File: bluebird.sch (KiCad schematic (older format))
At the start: 34 parts, among them J1 USB_C_Receptacle_USB2.0, J3 Conn_01x05, J4 Conn_01x01, J5 Conn_01x01, J6 AVR-ISP-6, J7 Conn_01x04, SW1 SW_PUSH, U1 ATMEGA32U4, U2 MCP23017_SS, U3 IS31FL3731-SA, Y1 FA328 16MHz

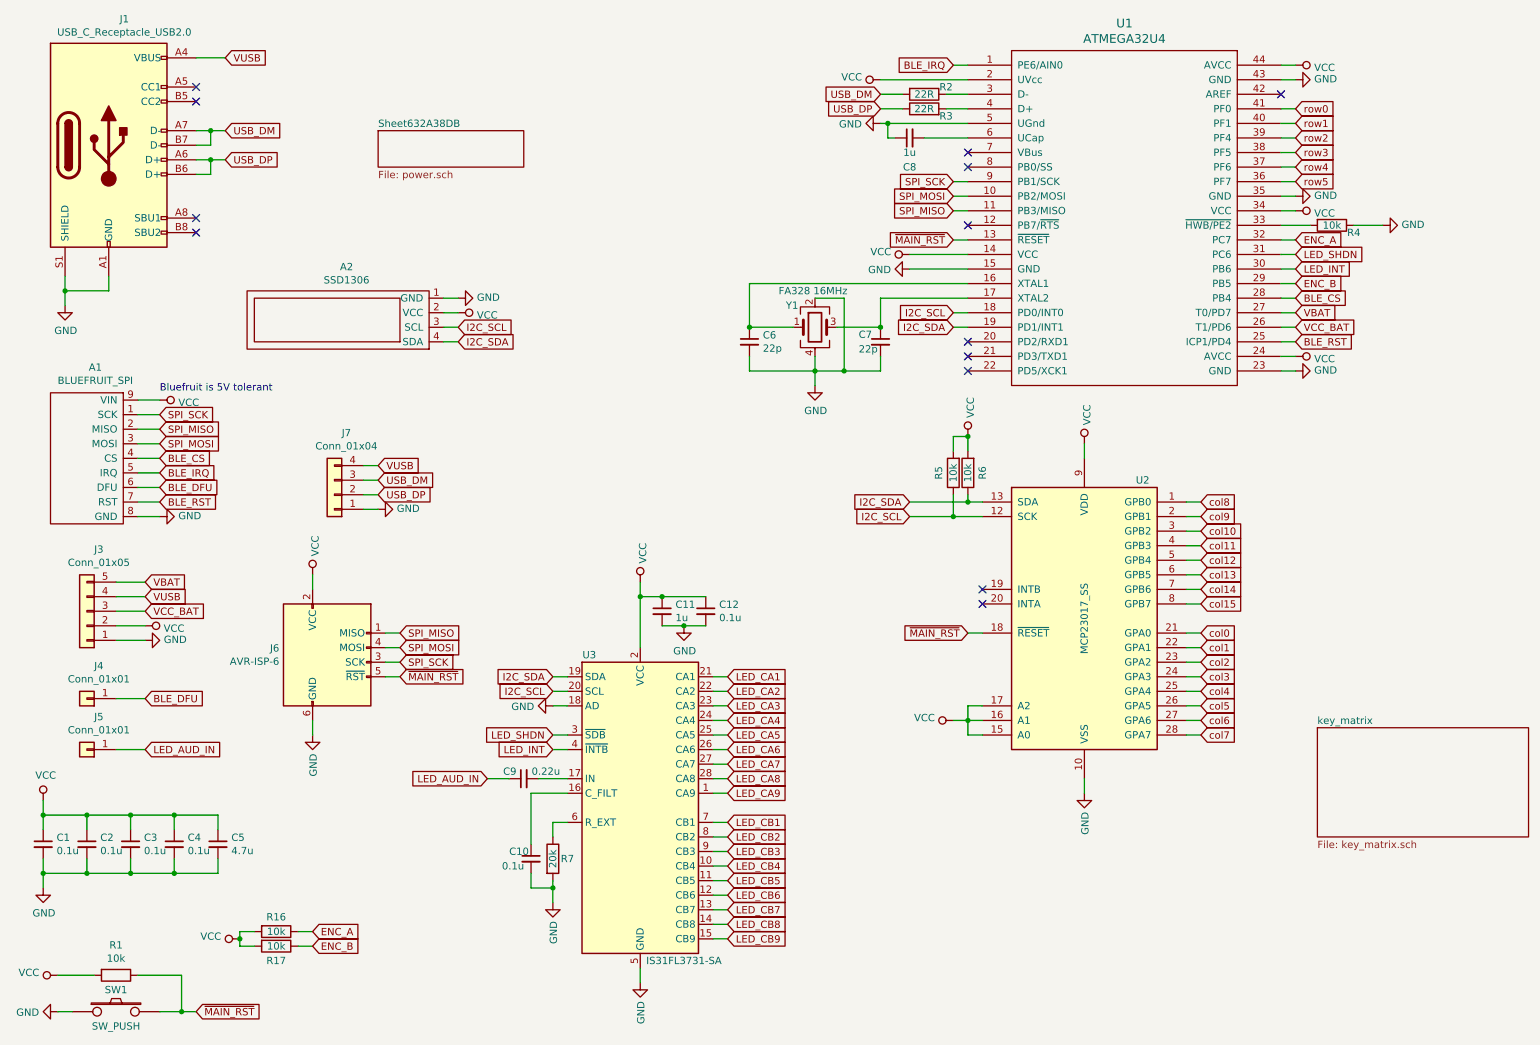
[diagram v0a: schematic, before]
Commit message: Rewire as 2 layer numpad
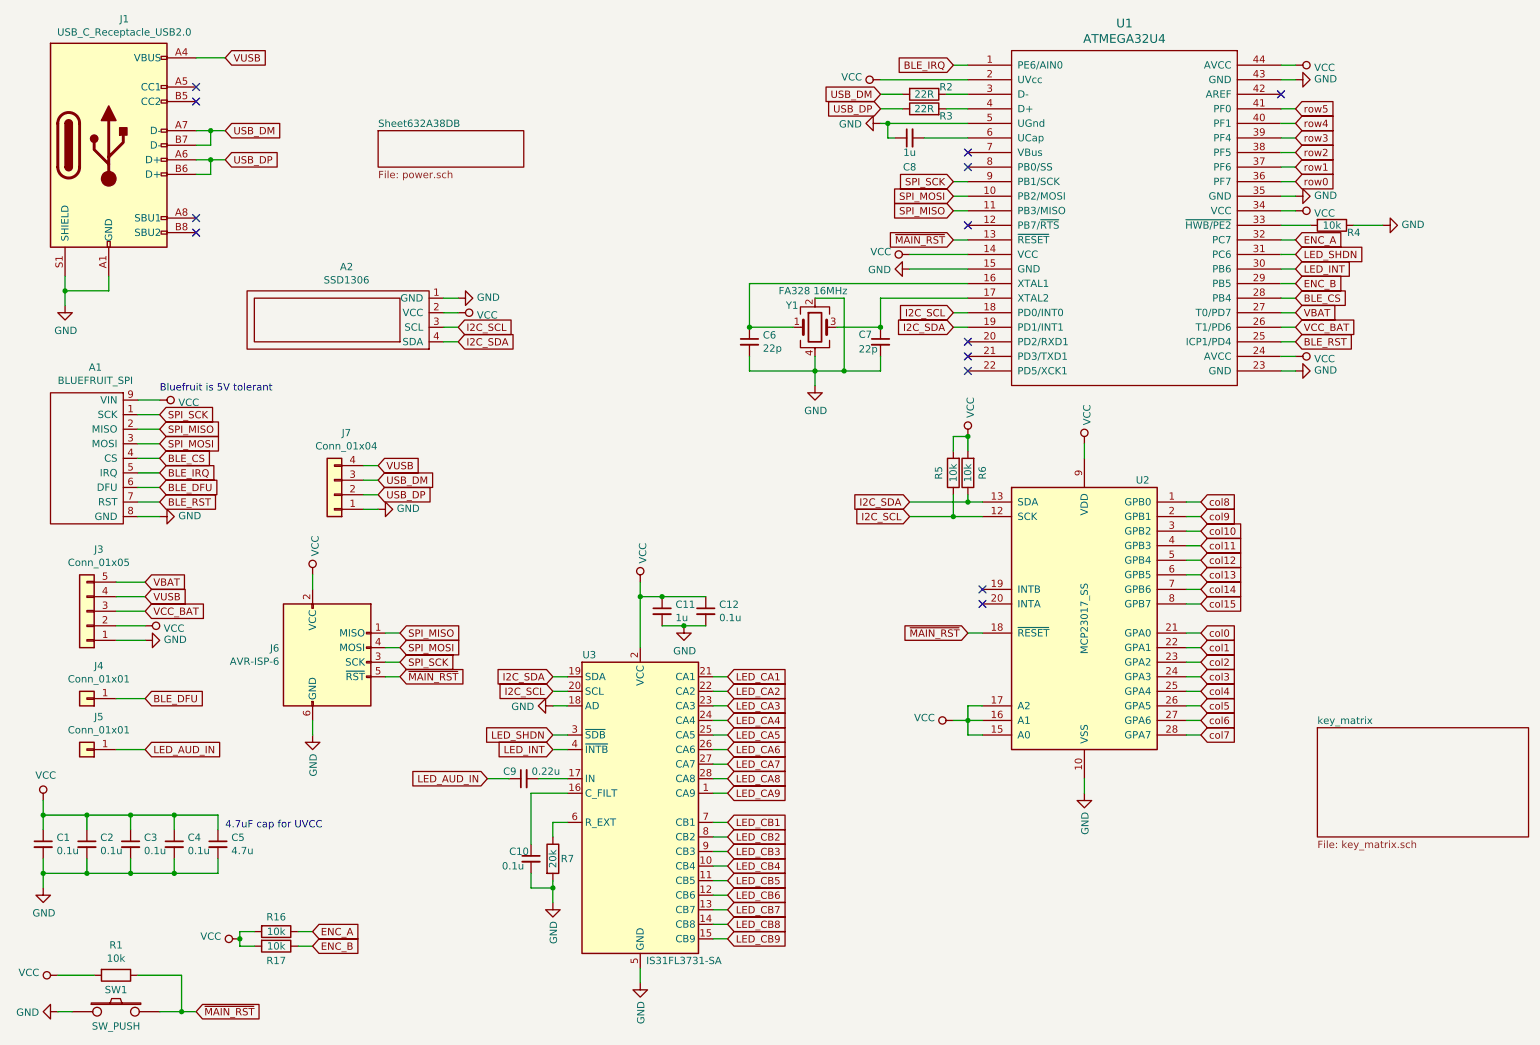
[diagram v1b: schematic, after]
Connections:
- net row0: now also U1.36 (PF7); no longer U1.41 (PF0)
- net row1: now also U1.37 (PF6); no longer U1.40 (PF1)
- net row2: now also U1.38 (PF5); no longer U1.39 (PF4)
- net row3: now also U1.39 (PF4); no longer U1.38 (PF5)
- net row4: now also U1.40 (PF1); no longer U1.37 (PF6)
- net row5: now also U1.41 (PF0); no longer U1.36 (PF7)
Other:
- note added: "4.7uF cap for UVCC"
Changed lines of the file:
@@
 F1 "key_matrix.sch" 50
 $EndSheet
-Text GLabel 9400 1500 2    50   Input ~ 0
+Text GLabel 9400 1800 2    50   Input ~ 0
 row1
 Wire Wire Line
@@
 	1    0    0    -1
 $EndComp
+Text GLabel 9400 1700 2    50   Input ~ 0
+row2
 Text GLabel 9400 1600 2    50   Input ~ 0
-row2
-Text GLabel 9400 1700 2    50   Input ~ 0
 row3
-Text GLabel 9400 1800 2    50   Input ~ 0
+Text GLabel 9400 1500 2    50   Input ~ 0
 row4
-Text GLabel 9400 1900 2    50   Input ~ 0
+Text GLabel 9400 1400 2    50   Input ~ 0
 row5
 Wire Wire Line
@@
 Wire Wire Line
 	7050 5600 7150 5600
-Text GLabel 9400 1400 2    50   Input ~ 0
+Text GLabel 9400 1900 2    50   Input ~ 0
 row0
 $Comp
@@
 Wire Wire Line
 	9300 2900 9400 2900
+Text Notes 2050 6350 0    50   ~ 0
+4.7uF cap for UVCC
 $EndSCHEMATC

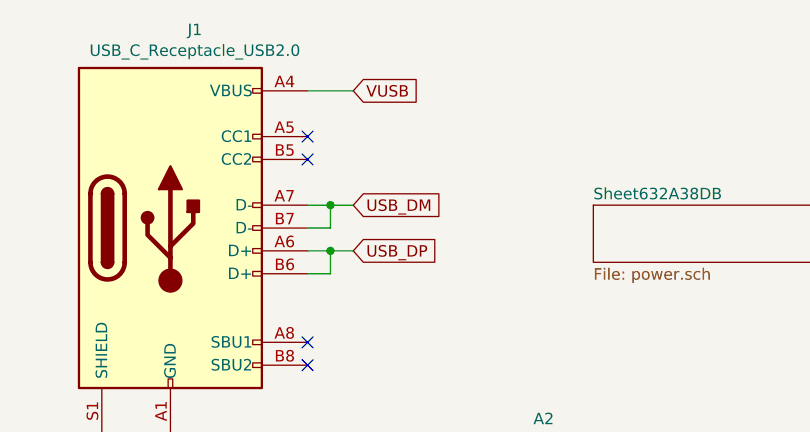
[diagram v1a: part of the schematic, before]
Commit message: Add USB C CC1/CC2 resistors, fix net overlaps.
Add labels to testpoints.
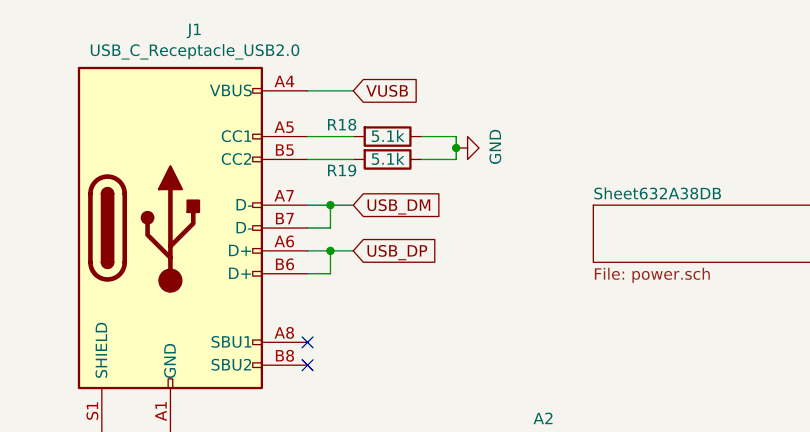
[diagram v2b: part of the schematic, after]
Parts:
- added R18, R19: 5.1k, Resistor_SMD:R_0805_2012Metric_Pad1.15x1.40mm_HandSolder, symbol Device:R
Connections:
- net GND: now also R18.1, R19.1
- net at J1.A5 (CC1): now also R18.2
- net at J1.B5 (CC2): now also R19.2
- no-connect marks 13 -> 11
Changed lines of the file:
@@
 NoConn ~ 1850 2150
 NoConn ~ 1850 2250
-NoConn ~ 1850 1350
-NoConn ~ 1850 1250
 Wire Wire Line
 	4300 5700 4400 5700
@@
 Text Notes 2050 6350 0    50   ~ 0
 4.7uF cap for UVCC
+$Comp
+L Device:R R18
+U 1 1 5EE4669E
+P 2200 1250
+F 0 "R18" V 2150 1050 50  0000 C CNN
+F 1 "5.1k" V 2200 1250 50  0000 C CNN
+F 2 "Resistor_SMD:R_0805_2012Metric_Pad1.15x1.40mm_HandSolder" V 2130 1250 50  0001 C CNN
+F 3 "~" H 2200 1250 50  0001 C CNN
+	1    2200 1250
+	0    1    1    0
+$EndComp
+$Comp
+L Device:R R19
+U 1 1 5EE46F2F
+P 2200 1350
+F 0 "R19" V 2250 1150 50  0000 C CNN
+F 1 "5.1k" V 2200 1350 50  0000 C CNN
+F 2 "Resistor_SMD:R_0805_2012Metric_Pad1.15x1.40mm_HandSolder" V 2130 1350 50  0001 C CNN
+F 3 "~" H 2200 1350 50  0001 C CNN
+	1    2200 1350
+	0    1    1    0
+$EndComp
+Wire Wire Line
+	1850 1250 2050 1250
+Wire Wire Line
+	1850 1350 2050 1350
+$Comp
+L power:GND #PWR0111
+U 1 1 5EE66D29
+P 2500 1300
+F 0 "#PWR0111" H 2500 1050 50  0001 C CNN
+F 1 "GND" H 2505 1127 50  0000 C CNN
+F 2 "" H 2500 1300 50  0001 C CNN
+F 3 "" H 2500 1300 50  0001 C CNN
+	1    2500 1300
+	0    -1   -1   0
+$EndComp
+Wire Wire Line
+	2350 1250 2500 1250
+Wire Wire Line
+	2500 1250 2500 1300
+Wire Wire Line
+	2350 1350 2500 1350
+Wire Wire Line
+	2500 1350 2500 1300
+Connection ~ 2500 1300
 $EndSCHEMATC
